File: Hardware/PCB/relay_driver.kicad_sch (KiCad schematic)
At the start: 5 parts, among them J5 Relay Terminal, Q1 MMBT2222A

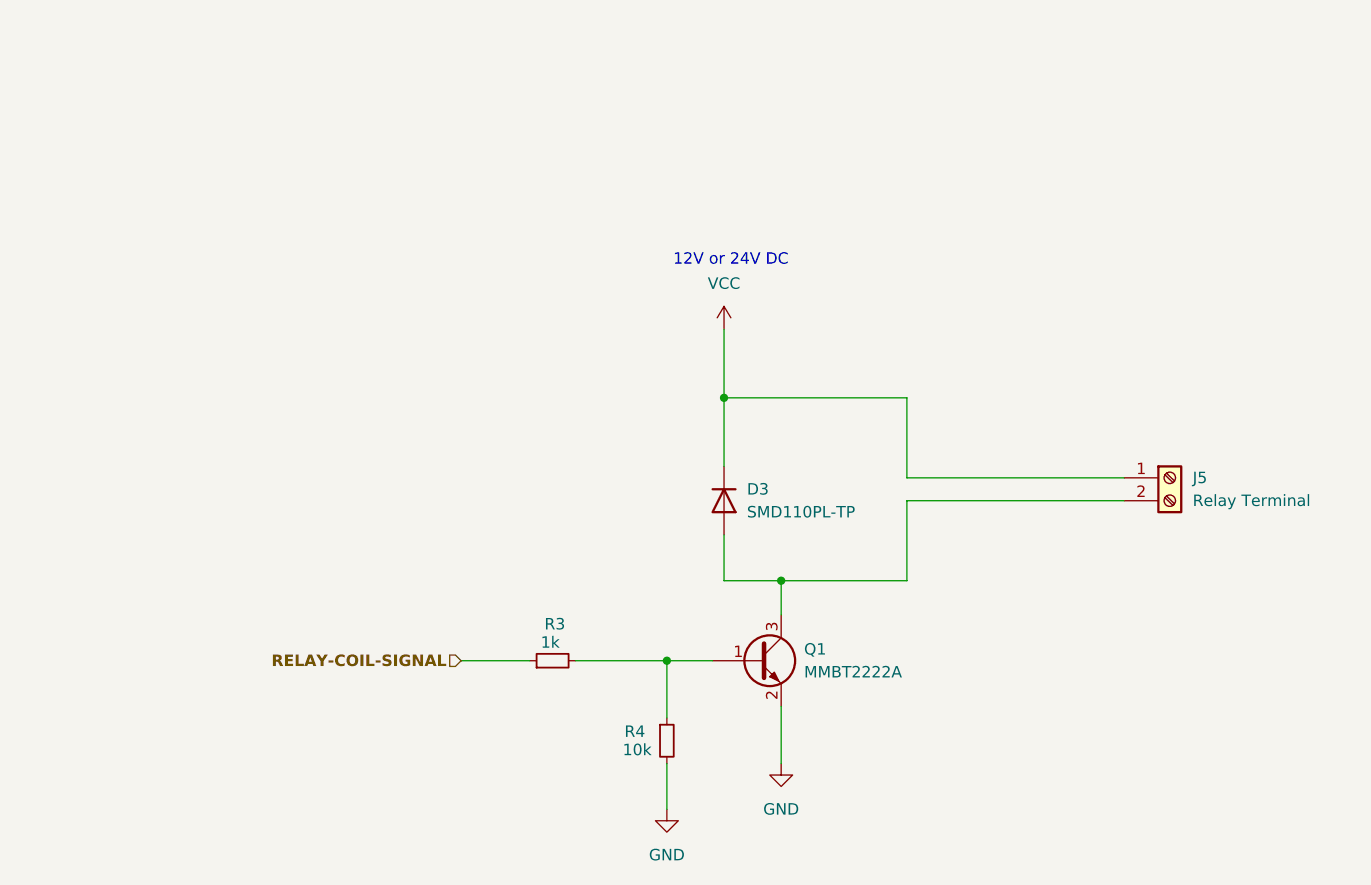
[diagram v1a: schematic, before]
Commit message: Added brushless DC support, fixed terminal blocks too
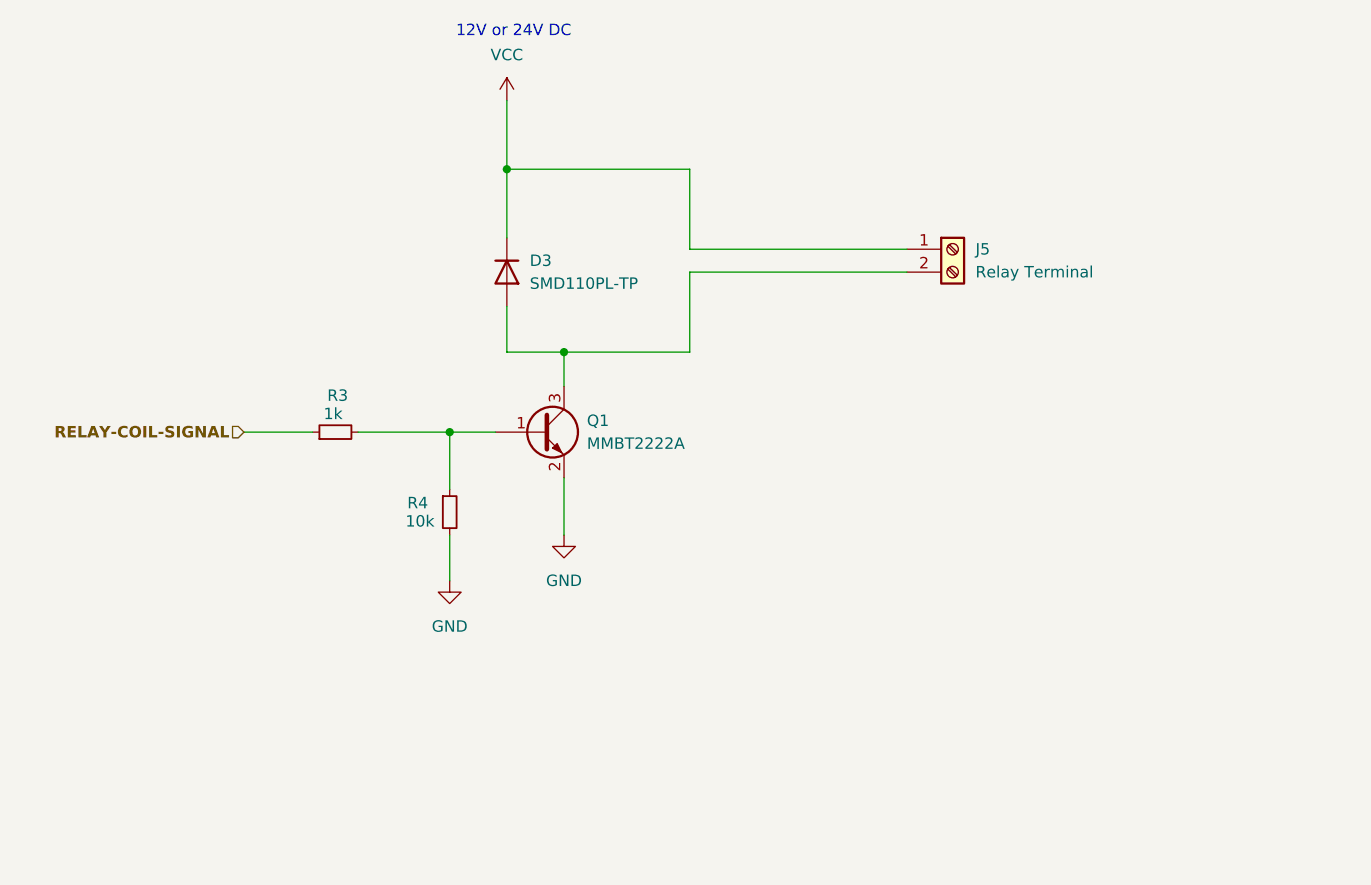
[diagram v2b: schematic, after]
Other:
- moved on the sheet: D3, J5, Q1, R3, R4

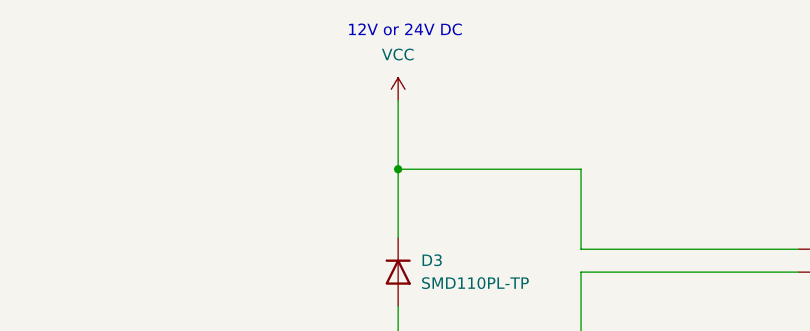
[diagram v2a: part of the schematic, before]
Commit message: switched to making buck converter to save costs and space, and to allow for LDO after 5.5V for better stability
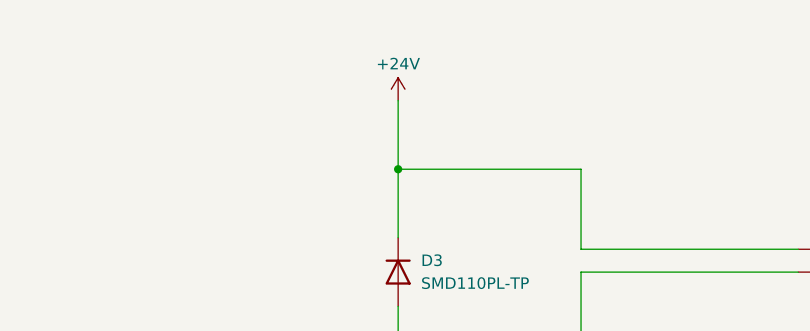
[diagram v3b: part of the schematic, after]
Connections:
- net VCC renamed +24V
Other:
- note removed: "12V or 24V DC"
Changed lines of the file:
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@@
-		)
-	)
-	(text "12V or 24V DC"
-		(exclude_from_sim no)
-		(at 98.552 25.4 0)
-		(effects
-			(font
-				(size 1.27 1.27)
-			)
 		)
 	)
@@
 	)
 	(symbol
-		(lib_id "power:VCC")
-		(at 97.79 33.02 0)
-		(unit 1)
-		(exclude_from_sim no)
-		(in_bom yes)
-		(on_board yes)
-		(dnp no)
-		(fields_autoplaced yes)
-		(property "Reference" "#PWR046"
-			(at 97.79 36.83 0)
-			(effects
-				(font
-					(size 1.27 1.27)
-				)
-				(hide yes)
-			)
-		)
-		(property "Value" "VCC"
-			(at 97.79 27.94 0)
-			(effects
-				(font
-					(size 1.27 1.27)
-				)
-			)
-		)
-		(property "Footprint" ""
-			(at 97.79 33.02 0)
-			(effects
-				(font
-					(size 1.27 1.27)
-				)
-				(hide yes)
-			)
-		)
-		(property "Datasheet" ""
-			(at 97.79 33.02 0)
-			(effects
-				(font
-					(size 1.27 1.27)
-				)
-				(hide yes)
-			)
-		)
-		(property "Description" "Power symbol creates a global label with name \"VCC\""
-			(at 97.79 33.02 0)
-			(effects
-				(font
-					(size 1.27 1.27)
-				)
-				(hide yes)
-			)
-		)
-		(pin "1"
-		)
-		(instances
-			(project "PCB"
-				(path "/c3756407-a933-418d-a16a-ea4e5b091ef7/8f472cc7-0cdc-4363-8965-a201b46c7d86"
-					(reference "#PWR046")
-					(unit 1)
-				)
-			)
-		)
-	)
-	(symbol
 		(lib_id "power:GND")
 		(at 104.14 81.28 0)
@@
 					(unit 1)
 				)
+			)
+		)
+	)
+	(symbol
+		(lib_id "power:+24V")
+		(at 97.79 33.02 0)
+		(unit 1)
+		(exclude_from_sim no)
+		(in_bom yes)
+		(on_board yes)
+		(dnp no)
+		(property "Reference" "#PWR033"
+			(at 97.79 36.83 0)
+			(effects
+				(font
+					(size 1.27 1.27)
+				)
+				(hide yes)
+			)
+		)
+		(property "Value" "+24V"
+			(at 97.79 28.956 0)
+			(effects
+				(font
+					(size 1.27 1.27)
+				)
+			)
+		)
+		(property "Footprint" ""
+			(at 97.79 33.02 0)
+			(effects
+				(font
+					(size 1.27 1.27)
+				)
+				(hide yes)
+			)
+		)
+		(property "Datasheet" ""
+			(at 97.79 33.02 0)
+			(effects
+				(font
+					(size 1.27 1.27)
+				)
+				(hide yes)
+			)
+		)
+		(property "Description" "Power symbol creates a global label with name \"+24V\""
+			(at 97.79 33.02 0)
+			(effects
+				(font
+					(size 1.27 1.27)
+				)
+				(hide yes)
+			)
+		)
+		(pin "1"
+		)
+		(instances
+			(project "PCB"
+				(path "/c3756407-a933-418d-a16a-ea4e5b091ef7/8f472cc7-0cdc-4363-8965-a201b46c7d86"
+					(reference "#PWR033")
+					(unit 1)
+				)

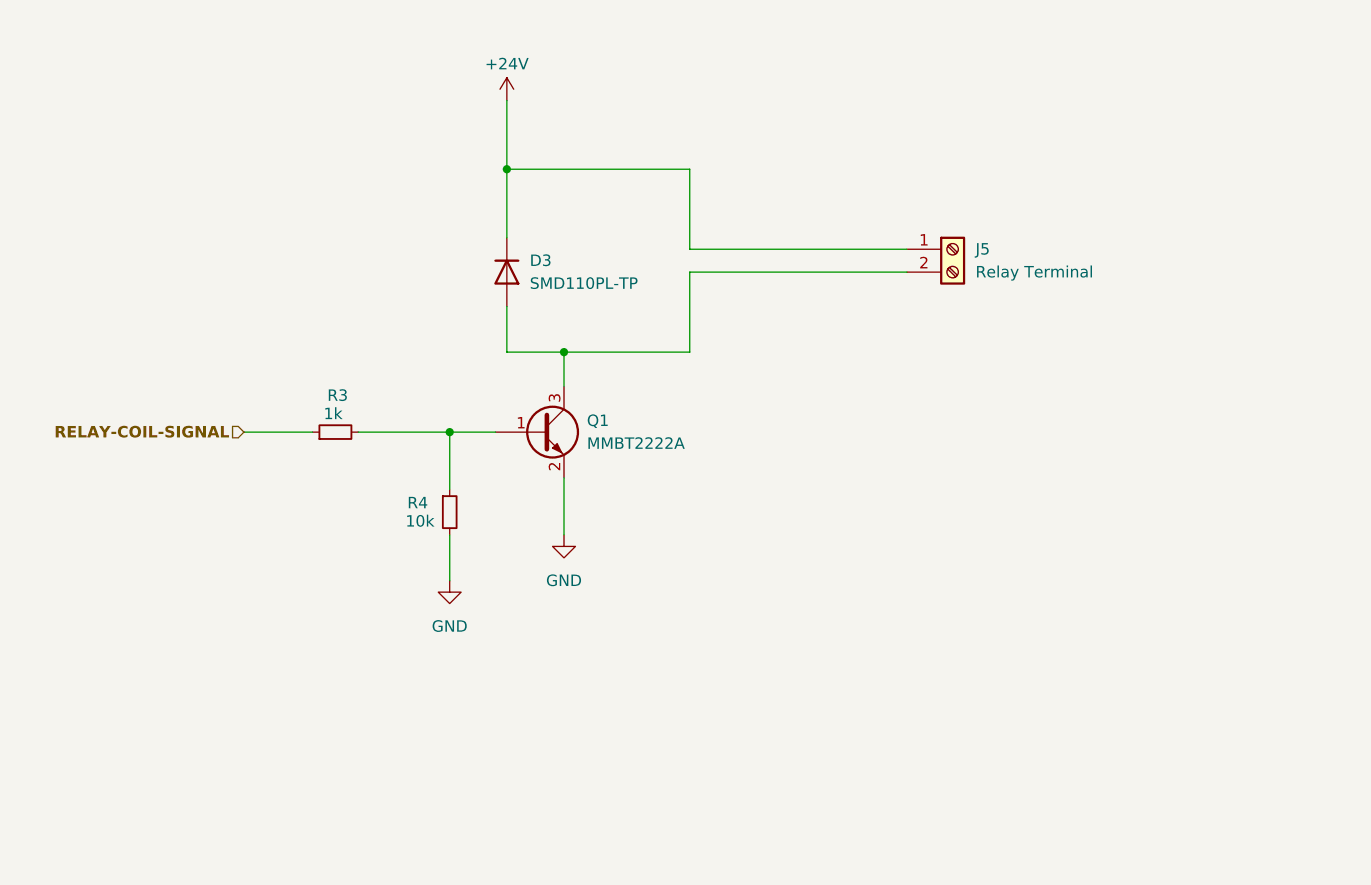
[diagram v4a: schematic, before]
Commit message: overall design is pretty much done, starting layout and routing now
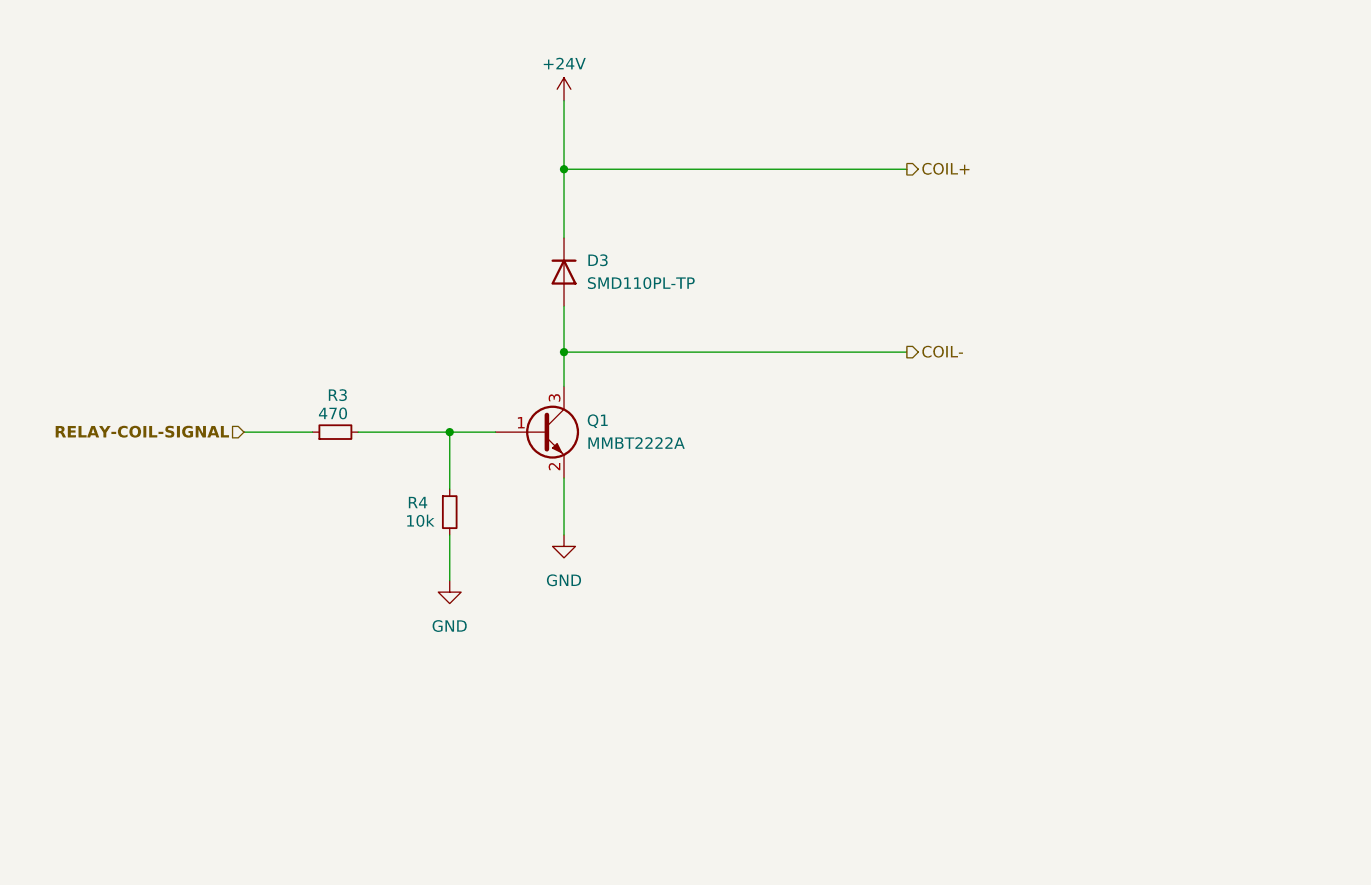
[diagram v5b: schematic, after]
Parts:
- removed J5: Relay Terminal, Vendor_Footprints:PHOENIX_1984963, symbol Connector:Screw_Terminal_01x02
- R3: value 1k -> 470; DigiKey Link https://www.digikey.com/en/products/detail/yageo/RC0603FR-0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 -> https://www.digikey.com/en/products/detail/yageo/RC0603JR-0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; MPN RC0603FR-071KL -> RC0603JR-07470RL
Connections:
- net COIL-: now reaches D3.2 (A), Q1.3 (C)
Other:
- moved on the sheet: D3

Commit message: kinda pricey, I should try to make a smaller version using LCSC parts for cheaper solution
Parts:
- D3: LCSC (none) -> C669053
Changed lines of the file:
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@@
+			)
+		)
+		(property "LCSC" ""
+			(at 78.74 69.85 0)
+			(effects
+				(font
+					(size 1.27 1.27)
+				)
 			)
 		)
@@
 			)
 		)
+		(property "LCSC" "C669053"
+			(at 104.14 52.07 0)
+			(effects
+				(font
+					(size 1.27 1.27)
+				)
+			)
+		)
 		(pin "1"
 		)
@@
 			)
 		)
+		(property "LCSC" ""
+			(at 91.44 78.74 0)
+			(effects
+				(font
+					(size 1.27 1.27)
+				)
+			)
+		)
 		(pin "1"
 		)
@@
 			)
 		)
+		(property "LCSC" ""
+			(at 101.6 69.85 0)
+			(effects
+				(font
+					(size 1.27 1.27)
+				)
+			)
+		)

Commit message: done with this, placed order
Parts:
- removed D3: SMD110PL-TP, Diode_SMD:D_SOD-123F, symbol Device:D
- added D9: SS310, Diode_SMD:D_SMA, symbol Device:D_Schottky
- added J7: Solenoid Terminal, Vendor_Footprints:CONN_WJ15EDGRC-3.81-2P, symbol Connector:Screw_Terminal_01x02
- Q1: LCSC (none) -> C916372
- R3: LCSC (none) -> C2907172; MPN RC0603JR-07470RL -> FRC0603J471 TS; Manufacturer YAGEO -> FOJAN
- R4: LCSC (none) -> C2930027; MPN RMCF0603JT10K0 -> FRC0603J103TS; Manufacturer Stackpole Electronics Inc -> FOJAN
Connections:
- net +24V: now also D9.1 (K), J7.1 (Pin_1)
- net COIL-: no longer names the net of Q1.3 (C)
- net COIL-: now also D9.2 (A), J7.2 (Pin_2)
